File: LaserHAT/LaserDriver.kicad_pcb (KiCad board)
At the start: 2 copper layers, 65 x 56 mm, 5 parts, among them J1 GPIO

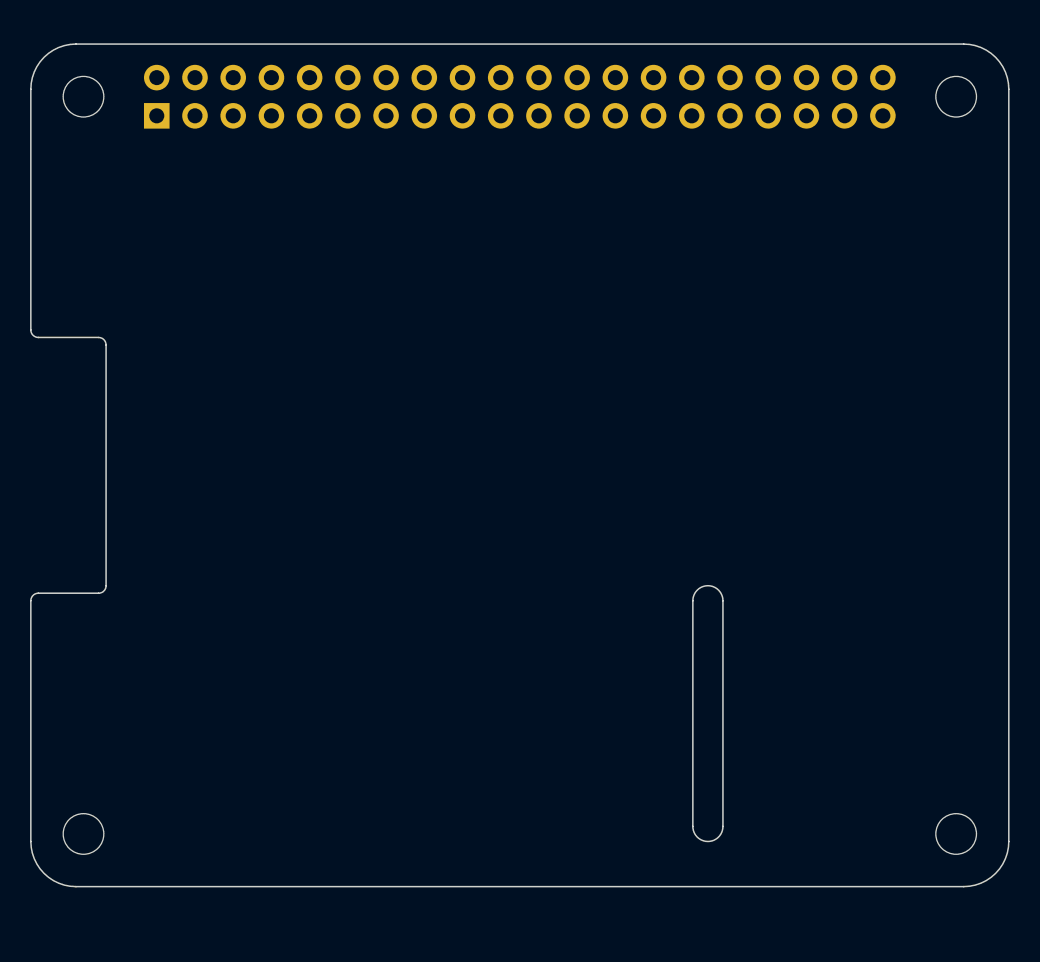
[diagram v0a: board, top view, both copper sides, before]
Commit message: Updates to design, finalized PCB layout
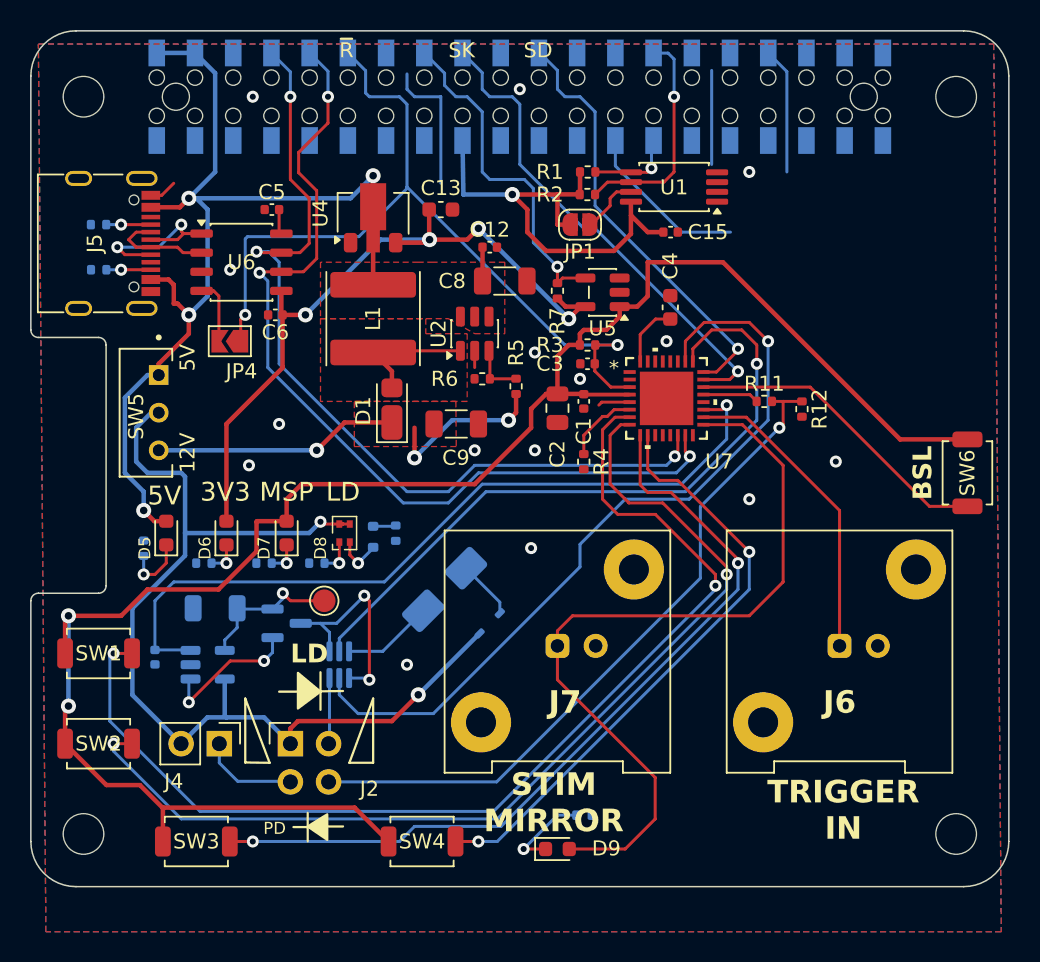
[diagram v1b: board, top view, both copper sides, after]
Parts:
- added C1: 100nF, Capacitor_SMD:C_0402_1005Metric, F.Cu at (136.8, 67.8)
- added C11: 10nF, Capacitor_SMD:C_0402_1005Metric, B.Cu at (108.2, 84.8)
- added C12: 100nF Ceramic, Capacitor_SMD:C_0402_1005Metric, F.Cu at (130.5, 57.5)
- added C13: 1uF Ceramic, Capacitor_SMD:C_0603_1608Metric, F.Cu at (127.2, 55.0)
- added C15: 100n, Capacitor_SMD:C_0402_1005Metric, F.Cu at (142.5, 56.5)
- added C2: 10uF, Capacitor_SMD:C_0805_2012Metric, F.Cu at (135.0, 68.2)
- added C3: 10nF, Capacitor_SMD:C_0402_1005Metric, F.Cu at (137.0, 65.2)
- added C4: 0.47uF, Capacitor_SMD:C_0603_1608Metric, F.Cu at (142.5, 61.5)
- added C5: 100nF, Capacitor_SMD:C_0402_1005Metric, F.Cu at (116.0, 55.0)
- added C6: 100nF, Capacitor_SMD:C_0402_1005Metric, F.Cu at (116.2, 62.0)
- added C8: 22µF 10V, Capacitor_SMD:C_1206_3216Metric, F.Cu at (131.5, 59.8)
- added C9: 22µF 16V, Capacitor_SMD:C_1206_3216Metric, F.Cu at (128.3, 69.2)
- added D1: SS14, Diode_SMD:D_SOD-123F, F.Cu at (124.0, 68.2)
- added D10: D_Zener 6.2V, Diode_SMD:D_SOD-523, B.Cu at (122.8, 76.8)
- added D2: Zener 4.7V, 1.5W, Diode_SMD:D_SMA, B.Cu at (127.5, 80.2)
- added D3: 1N4148W, Footprints:D_SOD-323F, B.Cu at (130.5, 82.5)
- added D5: 5V, Diode_SMD:D_0603_1608Metric, F.Cu at (109.0, 76.5)
- added D6: 3v3, Diode_SMD:D_0603_1608Metric, F.Cu at (113.0, 76.5)
- added D7: MSPM0, Diode_SMD:D_0603_1608Metric, F.Cu at (117.0, 76.5)
- added D8: LED_Dual_AKAK, LED_SMD:LED_LiteOn_LTST-C295K_1.6x0.8mm, F.Cu at (120.8, 76.5)
- added D9: STIM, Diode_SMD:D_0603_1608Metric, F.Cu at (135.0, 97.5)
- added J2: Conn_02x02_Counter_Clockwise, Connector_PinHeader_2.54mm:PinHeader_2x02_P2.54mm_Vertical, F.Cu at (117.2, 90.5)
- added J4: Jumper for 4-terminal diode configuration, Connector_PinHeader_2.54mm:PinHeader_1x02_P2.54mm_Vertical, F.Cu at (112.5, 90.5)
- added J5: USB_C_Receptacle_USB2.0_16P, Connector_USB:USB_C_Receptacle_G-Switch_GT-USB-7010ASV, F.Cu at (104.2, 57.2)
- added J6: Conn_Coaxial, Connector_Coaxial:BNC_Amphenol_031-5539_Vertical, F.Cu at (153.8, 84.0)
- added J7: Conn_Coaxial, Connector_Coaxial:BNC_Amphenol_031-5539_Vertical, F.Cu at (135.0, 84.0)
- added JP1: ID_WP, Jumper:SolderJumper-2_P1.3mm_Open_RoundedPad1.0x1.5mm, F.Cu at (136.5, 56.0)
- added JP4: ID_WP, Jumper:SolderJumper-2_P1.3mm_Open_TrianglePad1.0x1.5mm, F.Cu at (113.2, 63.8)
- added L1: 22uH, Inductor_SMD:L_APV_ANR6045, F.Cu at (122.8, 62.2)
- added Q1: SI3134KDWA-TP, Package_TO_SOT_SMD:SOT-363_SC-70-6, B.Cu at (120.5, 85.2)
- added Q2: DMN2056U, Package_TO_SOT_SMD:SOT-23, B.Cu at (117.0, 82.5)
- added R1: 3.9k, Resistor_SMD:R_0402_1005Metric, F.Cu at (137.0, 52.5)
- added R10: 5.1K, Resistor_SMD:R_0402_1005Metric, B.Cu at (104.5, 59.0)
- added R11: 1k, Resistor_SMD:R_0402_1005Metric, F.Cu at (148.8, 67.8)
- added R12: 4.7k, Resistor_SMD:R_0402_1005Metric, F.Cu at (151.2, 68.3)
- added R13: 1k, Resistor_SMD:R_0402_1005Metric, B.Cu at (107.5, 77.5)
- added R14: 500, Resistor_SMD:R_0402_1005Metric, B.Cu at (111.5, 78.5)
- added R15: 1k, Resistor_SMD:R_0402_1005Metric, B.Cu at (115.5, 78.5)
- added R16: 500, Resistor_SMD:R_0402_1005Metric, B.Cu at (119.0, 78.5)
- added R17: 500, Resistor_SMD:R_0402_1005Metric, B.Cu at (124.2, 76.5)
- added R18: 500, Resistor_SMD:R_0402_1005Metric, B.Cu at (136.8, 95.2)
- added R2: 3.9k, Resistor_SMD:R_0402_1005Metric, F.Cu at (137.0, 54.0)
- added R3: 47K, Resistor_SMD:R_0402_1005Metric, F.Cu at (137.0, 64.0)
- added R4: 100K 0.1%, Resistor_SMD:R_0402_1005Metric, F.Cu at (136.8, 71.8)
- added R5: 187K 1%, Resistor_SMD:R_0402_1005Metric, F.Cu at (132.2, 66.8)
- added R6: 10K 1%, Resistor_SMD:R_0402_1005Metric, F.Cu at (130.0, 66.2)
- added R7: 10k, Resistor_SMD:R_0402_1005Metric, F.Cu at (135.0, 60.4)
- added R8: 5.1K, Resistor_SMD:R_0402_1005Metric, B.Cu at (104.5, 56.0)
- added Rs1: 10Ω 1%, Resistor_SMD:R_1206_3216Metric, B.Cu at (112.2, 81.5)
- added SW1: B, Button_Switch_SMD:SW_SPST_TS-1088-xR020, F.Cu at (104.5, 84.5)
- added SW2: B, Button_Switch_SMD:SW_SPST_TS-1088-xR020, F.Cu at (104.5, 90.5)
- added SW3: B, Button_Switch_SMD:SW_SPST_TS-1088-xR020, F.Cu at (111.0, 97.0)
- added SW4: B, Button_Switch_SMD:SW_SPST_TS-1088-xR020, F.Cu at (126.0, 97.0)
- added SW5: SW_SPDT, ELEC327-Kicad:SW_EG1270, F.Cu at (108.5, 68.5)
- added SW6: BSL, Button_Switch_SMD:SW_SPST_TS-1088-xR020, F.Cu at (162.2, 72.5)
- added TP1: TestPoint, TestPoint:TestPoint_Pad_D1.5mm, F.Cu at (119.5, 81.0)
- added U1: CAT24C32, Package_SO:TSSOP-8_4.4x3mm_P0.65mm, F.Cu at (142.8, 53.5)
- added U2: MT3608, Package_TO_SOT_SMD:SOT-23-6, F.Cu at (129.5, 63.2)
- added U3: TLV2371DBV, Package_TO_SOT_SMD:SOT-23-5, B.Cu at (111.8, 85.2)
- added U4: MCP1700x-330xxMB, Package_TO_SOT_SMD:SOT-89-3, F.Cu at (122.8, 55.2)
- added U5: AP2171W, Package_TO_SOT_SMD:SOT-23-5, F.Cu at (138.0, 60.5)
- added U6: CH340N, Package_SO:JEITA_SOIC-8_3.9x4.9mm_P1.27mm, F.Cu at (114.0, 58.5)
- added U7: MSPM0G3507SRHBR, ELEC327-Kicad:VQFN32_RHB_TEX, F.Cu at (142.2, 67.5)
- J1: footprint Connector_PinSocket_2.54mm:PinSocket_2x20_P2.54mm_Vertical -> Connector_Samtec_HLE_SMD:Samtec_HLE-120-02-xxx-DV-BE-LC_2x20_P2.54mm_Horizontal
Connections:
- net +3V3 renamed RPi +3V3
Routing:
- net MSPM0_3V3: track 0.00 -> 123.2 mm, vias 0 -> 2
- net /MSPM0 Controller/BUTTON1: track 0.00 -> 72.0 mm, vias 0 -> 2
- net +5V: track 0.00 -> 69.4 mm, vias 0 -> 4
- net LASER_V: track 0.00 -> 67.5 mm, vias 0 -> 2
- net /MSPM0 Controller/BUTTON2: track 0.00 -> 67.0 mm, vias 0 -> 2
- net /GPIO15/RXD0: track 0.00 -> 60.9 mm, vias 0 -> 3
- net /GPIO14/TXD0: track 0.00 -> 58.3 mm, vias 0 -> 3
- net /GPIO18/PCM.CLK: track 0.00 -> 55.2 mm, vias 0 -> 2
- net /MSPM0 Controller/BUTTON3: track 0.00 -> 54.6 mm, vias 0 -> 2
- net /STIM_MIRROR: track 0.00 -> 52.2 mm
- net /Laser Driver Circuit/PWM_DUMMY: track 0.00 -> 52.2 mm, vias 0 -> 1
- net /Laser Driver Circuit/LASER_VREF: track 0.00 -> 52.0 mm, vias 0 -> 1
- net +3V3: track 0.00 -> 48.7 mm, vias 0 -> 4
- net Net-(J2-PD_Anode): track 0.00 -> 46.3 mm, vias 0 -> 1
- net /Laser Driver Circuit/PWM_LASER: track 0.00 -> 45.6 mm, vias 0 -> 1
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- added copper zone on F.Cu, net +12V
- added copper zone on F.Cu, net +5V
- added copper zone on F.Cu, net /Laser Driver Circuit/SW
- added copper zone on B.Cu, net GND
- added copper zone on F.Cu, net GND
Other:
- board size 65 x 56 mm -> 65 x 56.9 mm
- board text added: "12V"
- board text added: "3V3"
- board text added: "5V"
- board text added: "BSL"
- board text added: "LD"
- board text added: "MSP"
- board text added: "PD"
- board text added: "SD"
- board text added: "SK"
- board text added: "STIM MIRROR"
- board text added: "TRIGGER IN"
- board text added: "~{R}"
- board text removed: "CAMERA (OPTIONAL)"
- board text removed: "PoE"

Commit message: Updated project for manufacturing. Should merge branch if/when we get back a working product
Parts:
- removed D8: LED_Dual_AKAK, LED_SMD:LED_LiteOn_LTST-C295K_1.6x0.8mm
- added D11: LED_ABGR, LED_SMD:LED_RGB_1210, F.Cu at (123.0, 76.5)
- added REF**: RICE_OWL_LOGO, ELEC327-Kicad:RICE_OWL_LOGO, F.Cu at (156.1, 63.4)
- C12: value 100nF Ceramic -> 100nF
- C13, C4: footprint Capacitor_SMD:C_0603_1608Metric -> Capacitor_SMD:C_0402_1005Metric
- C15: value 100n -> 100nF
- C8: value 22µF 10V -> 22µF 16V
- R10, R8: value 5.1K -> 5.1k
- R11: value 1k -> 1k 0.1%
- R13: value 1k -> 1k 1%
- R14: value 500 -> 200
- R15: value 1k -> 200
- R16, R18: value 500 -> 470
- R17: value 500 -> 1k 1%
- R3: value 47K -> 47k 1%
- R4: value 100K 0.1% -> 100k 0.1%
- R5: value 187K 1% -> 187k 1%
- R6: value 10K 1% -> 10k
- SW5: footprint ELEC327-Kicad:SW_EG1270 -> Button_Switch_SMD:SW_SPDT_PCM12
- moved R17 2.05 mm to (122.2, 76.6), turned to 90 degrees
- moved D10 1.30 mm to (124.0, 76.4), turned to 90 degrees
- moved SW5 1.14 mm to (107.5, 68.0)
- moved C13 0.77 mm to (127.2, 54.2), turned to 90 degrees
- moved C4 0.75 mm to (142.5, 62.2), turned to 0 degrees
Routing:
- net +5V: track 69.4 -> 72.9 mm
- net LASER_V: track 67.5 -> 66.0 mm, vias 2 -> 3
- net Net-(D10-A): track 3.09 -> 4.44 mm
- net Net-(D11-BK): track 2.38 -> 3.23 mm
- net MSPM0_3V3: track 123.2 -> 123.9 mm
- net +3V3: track 48.7 -> 49.2 mm
- net +12V: track 27.5 -> 27.4 mm, vias 3 -> 4
- net GND: vias 15 -> 16
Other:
- board text added: "(c) 2026"
- board text added: "CK SDG"
- board text added: "LaserHat v1.0 Kemere Lab"
